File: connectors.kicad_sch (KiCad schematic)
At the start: 4 parts

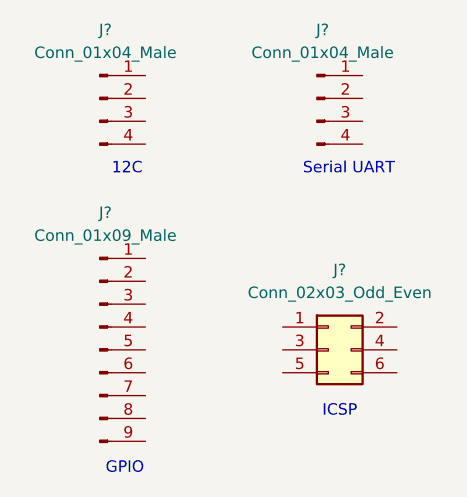
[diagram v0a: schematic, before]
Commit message: Added component values.
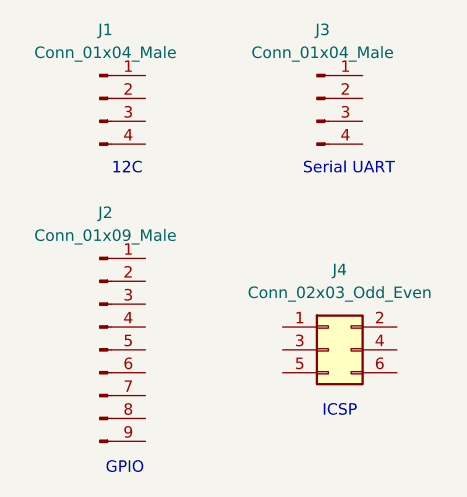
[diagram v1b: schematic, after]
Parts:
- gave numbers to parts that had none: 4
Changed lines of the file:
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@@
 		(dnp no)
 		(fields_autoplaced yes)
-		(property "Reference" "J?"
+		(property "Reference" "J2"
 			(at 114.935 101.6 0)
 			(effects
@@
 			(project ""
 				(path "/3f5b0a10-2d4e-4174-92fa-d46a20738e80/96d1fc6e-9d9f-4fd0-91b9-82b9adfa0f34"
-					(reference "J?")
+					(reference "J2")
 					(unit 1)
 				)
@@
 		(dnp no)
 		(fields_autoplaced yes)
-		(property "Reference" "J?"
+		(property "Reference" "J1"
 			(at 114.935 81.28 0)
 			(effects
@@
 			(project ""
 				(path "/3f5b0a10-2d4e-4174-92fa-d46a20738e80/96d1fc6e-9d9f-4fd0-91b9-82b9adfa0f34"
-					(reference "J?")
+					(reference "J1")
 					(unit 1)
 				)
@@
 		(dnp no)
 		(fields_autoplaced yes)
-		(property "Reference" "J?"
+		(property "Reference" "J4"
 			(at 140.97 107.95 0)
 			(effects
@@
 			(project ""
 				(path "/3f5b0a10-2d4e-4174-92fa-d46a20738e80/96d1fc6e-9d9f-4fd0-91b9-82b9adfa0f34"
-					(reference "J?")
+					(reference "J4")
 					(unit 1)
 				)
@@
 		(dnp no)
 		(fields_autoplaced yes)
-		(property "Reference" "J?"
+		(property "Reference" "J3"
 			(at 139.065 81.28 0)
 			(effects
@@
 			(project ""
 				(path "/3f5b0a10-2d4e-4174-92fa-d46a20738e80/96d1fc6e-9d9f-4fd0-91b9-82b9adfa0f34"
-					(reference "J?")
-					(unit 1)
-				)
+					(reference "J3")
+					(unit 1)
+				)

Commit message: Completed symbol-footprint associations.
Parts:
- J1, J3: footprint (none) -> Connector_PinHeader_2.54mm:PinHeader_1x04_P2.54mm_Vertical
- J2: footprint (none) -> Connector_PinHeader_2.54mm:PinHeader_1x09_P2.54mm_Vertical
- J4: footprint (none) -> Connector_PinHeader_2.54mm:PinHeader_2x03_P2.54mm_Vertical
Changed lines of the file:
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@@
 			)
 		)
-		(property "Footprint" ""
+		(property "Footprint" "Connector_PinHeader_2.54mm:PinHeader_1x09_P2.54mm_Vertical"
 			(at 114.3 116.84 0)
 			(effects
@@
 			)
 		)
-		(property "Footprint" ""
+		(property "Footprint" "Connector_PinHeader_2.54mm:PinHeader_1x04_P2.54mm_Vertical"
 			(at 114.3 88.9 0)
 			(effects
@@
 			)
 		)
-		(property "Footprint" ""
+		(property "Footprint" "Connector_PinHeader_2.54mm:PinHeader_2x03_P2.54mm_Vertical"
 			(at 139.7 116.84 0)
 			(effects
@@
 			)
 		)
-		(property "Footprint" ""
+		(property "Footprint" "Connector_PinHeader_2.54mm:PinHeader_1x04_P2.54mm_Vertical"
 			(at 138.43 88.9 0)
 			(effects
